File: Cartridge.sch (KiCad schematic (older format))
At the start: 1 part, among them J4 Expansion

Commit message: MMU, Joy, Cart and Video
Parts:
- added C18: 100nF, Atari:C_Axial_L5.1mm_D2.5mm_P12.50mm_Horizontal, symbol Device:C
- added J24: Cartridge, Atari:Cartridge_Slot, symbol Atari:Cartridge
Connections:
- net GND: now also C18.2, J24.B (GND)
- new net +5P: C18.1, J24.13 (VCC)
- new net A0: J24.5 (A0)
- new net A1: J24.4 (A1)
- new net A10: J24.P (A10)
- new net A11: J24.N (A11)
- new net A12: J24.K (A12)
- new net A2: J24.3 (A2)
- new net A3: J24.2 (A3)
- new net A4: J24.C (A4)
- new net A5: J24.D (A5)
- new net A6: J24.E (A6)
- new net A7: J24.F (A7)
- new net A8: J24.H (A8)
- new net A9: J24.J (A9)
- new net BO2: J24.S (O2)
- new net CCTL: J24.15 (~CCTL)
- new net D0: J24.10 (D0)
- new net D1: J24.9 (D1)
- new net D2: J24.8 (D2)
- new net D3: J24.L (D3)
- new net D4: J24.6 (D4)
- new net D5: J24.7 (D5)
- new net D6: J24.11 (D6)
- new net D7: J24.M (D7)
- new net RD4: J24.A (RD4)
- new net RD5: J24.14 (RDS)
- new net RW: J24.R (R/~W)
- new net S4: J24.1 (~S4)
- new net S5: J24.12 (~S5)
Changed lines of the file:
@@
 $Descr A4 11693 8268
 encoding utf-8
-Sheet 7 14
+Sheet 7 15
 Title ""
 Date ""
@@
 Wire Wire Line
 	3125 3950 3125 3750
+$Comp
+L Atari:Cartridge J24
+U 1 1 602F6C5A
+P 6700 3500
+F 0 "J24" H 6783 5215 50  0000 C CNN
+F 1 "Cartridge" H 6783 5124 50  0000 C CNN
+F 2 "Atari:Cartridge_Slot" H 7100 3450 50  0001 C CNN
+F 3 "" H 7100 3450 50  0001 C CNN
+	1    6700 3500
+	1    0    0    -1
+$EndComp
+Text GLabel 7000 2050 2    50   Input ~ 0
+A0
+Text GLabel 7000 2150 2    50   Input ~ 0
+A1
+Text GLabel 7000 2250 2    50   Input ~ 0
+A2
+Text GLabel 7000 2350 2    50   Input ~ 0
+A3
+Text GLabel 7000 2450 2    50   Input ~ 0
+A4
+Text GLabel 7000 2550 2    50   Input ~ 0
+A5
+Text GLabel 7000 2650 2    50   Input ~ 0
+A6
+Text GLabel 7000 2750 2    50   Input ~ 0
+A7
+Text GLabel 7000 2850 2    50   Input ~ 0
+A8
+Text GLabel 7000 2950 2    50   Input ~ 0
+A9
+Text GLabel 7000 3050 2    50   Input ~ 0
+A10
+Text GLabel 7000 3150 2    50   Input ~ 0
+A11
+Text GLabel 7000 3250 2    50   Input ~ 0
+A12
+Text GLabel 7000 3350 2    50   Input ~ 0
+D0
+Text GLabel 7000 3450 2    50   Input ~ 0
+D1
+Text GLabel 7000 3550 2    50   Input ~ 0
+D2
+Text GLabel 7000 3650 2    50   Input ~ 0
+D3
+Text GLabel 7000 3750 2    50   Input ~ 0
+D4
+Text GLabel 7000 3850 2    50   Input ~ 0
+D5
+Text GLabel 7000 3950 2    50   Input ~ 0
+D6
+Text GLabel 7000 4050 2    50   Input ~ 0
+D7
+Text GLabel 7000 4150 2    50   Input ~ 0
+S4
+Text GLabel 7000 4250 2    50   Input ~ 0
+S5
+Text GLabel 7000 4350 2    50   Input ~ 0
+RD5
+Text GLabel 7000 4450 2    50   Input ~ 0
+RD4
+Text GLabel 7000 4550 2    50   Input ~ 0
+CCTL
+Text GLabel 7000 4650 2    50   Input ~ 0
+RW
+Text GLabel 7000 4750 2    50   Input ~ 0
+BO2
+$Comp
+L power:+5P #PWR0197
+U 1 1 602F9620
+P 7475 4775
+F 0 "#PWR0197" H 7475 4625 50  0001 C CNN
+F 1 "+5P" H 7490 4948 50  0000 C CNN
+F 2 "" H 7475 4775 50  0001 C CNN
+F 3 "" H 7475 4775 50  0001 C CNN
+	1    7475 4775
+	1    0    0    -1
+$EndComp
+$Comp
+L Device:C C18
+U 1 1 602F9DE7
+P 7475 5000
+F 0 "C18" H 7590 5046 50  0000 L CNN
+F 1 "100nF" H 7590 4955 50  0000 L CNN
+F 2 "Atari:C_Axial_L5.1mm_D2.5mm_P12.50mm_Horizontal" H 7513 4850 50  0001 C CNN
+F 3 "~" H 7475 5000 50  0001 C CNN
+	1    7475 5000
+	1    0    0    -1
+$EndComp
+Wire Wire Line
+	7000 4850 7475 4850
+Wire Wire Line
+	7475 4775 7475 4850
+Connection ~ 7475 4850
+Wire Wire Line
+	7000 4950 7000 5150
+Wire Wire Line
+	7000 5150 7475 5150
+$Comp
+L power:GND #PWR0198
+U 1 1 602FAB68
+P 7475 5275
+F 0 "#PWR0198" H 7475 5025 50  0001 C CNN
+F 1 "GND" H 7480 5102 50  0000 C CNN
+F 2 "" H 7475 5275 50  0001 C CNN
+F 3 "" H 7475 5275 50  0001 C CNN
+	1    7475 5275
+	1    0    0    -1
+$EndComp
+Wire Wire Line
+	7475 5150 7475 5275
+Connection ~ 7475 5150
 $EndSCHEMATC

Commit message: Tracking
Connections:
- net +5P is gone; now on net +5VA: C18.1, J24.13 (VCC)
- net AUD renamed AUDIO
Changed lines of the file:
@@
 MPD
 Text GLabel 2650 3850 2    50   Input ~ 0
-AUD
+AUDIO
 $Comp
 L power:GND #PWR0143
@@
 BO2
 $Comp
-L power:+5P #PWR0197
-U 1 1 602F9620
-P 7475 4775
-F 0 "#PWR0197" H 7475 4625 50  0001 C CNN
-F 1 "+5P" H 7490 4948 50  0000 C CNN
-F 2 "" H 7475 4775 50  0001 C CNN
-F 3 "" H 7475 4775 50  0001 C CNN
-	1    7475 4775
-	1    0    0    -1
-$EndComp
-$Comp
 L Device:C C18
 U 1 1 602F9DE7
@@
 	7475 5150 7475 5275
 Connection ~ 7475 5150
+$Comp
+L power:+5VA #PWR0197
+U 1 1 602ED419
+P 7475 4775
+F 0 "#PWR0197" H 7475 4625 50  0001 C CNN
+F 1 "+5VA" H 7490 4948 50  0000 C CNN
+F 2 "" H 7475 4775 50  0001 C CNN
+F 3 "" H 7475 4775 50  0001 C CNN
+	1    7475 4775
+	1    0    0    -1
+$EndComp
 $EndSCHEMATC

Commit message: Tracking
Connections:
- net AUDIO renamed EXTAUDIO
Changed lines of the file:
@@
 MPD
 Text GLabel 2650 3850 2    50   Input ~ 0
-AUDIO
+EXTAUDIO
 $Comp
 L power:GND #PWR0143

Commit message: Diagnostic
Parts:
- added J212: Diag, Connector_PinHeader_2.54mm:PinHeader_2x05_P2.54mm_Vertical, symbol Connector_Generic:Conn_02x05_Odd_Even
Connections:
- net BO2: now also J212.1 (Pin_1)
- net CCTL: now also J212.3 (Pin_3)
- net D1XX: now also J212.4 (Pin_4)
- net GND: now also J212.10 (Pin_10)
- net RD4: now also J212.7 (Pin_7)
- net RD5: now also J212.2 (Pin_2)
- net RW: now also J212.8 (Pin_8)
- net S4: now also J212.5 (Pin_5)
- net S5: now also J212.9 (Pin_9)
- new net D6XX: J212.6 (Pin_6)
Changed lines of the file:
@@
+	1    0    0    -1
+$EndComp
+Text GLabel 5025 2900 2    50   Input ~ 0
+D1XX
+Text GLabel 4525 2800 0    50   Input ~ 0
+BO2
+Text GLabel 4525 2900 0    50   Input ~ 0
+CCTL
+Text GLabel 4525 3000 0    50   Input ~ 0
+S4
+Text GLabel 4525 3100 0    50   Input ~ 0
+RD4
+Text GLabel 4525 3200 0    50   Input ~ 0
+S5
+Text GLabel 5025 2800 2    50   Input ~ 0
+RD5
+Text GLabel 5025 3000 2    50   Input ~ 0
+D6XX
+Text GLabel 5025 3200 2    50   Input ~ 0
+GND
+Text GLabel 5025 3100 2    50   Input ~ 0
+RW
+$Comp
+L Connector_Generic:Conn_02x05_Odd_Even J212
+U 1 1 604245DE
+P 4725 3000
+F 0 "J212" H 4775 3417 50  0000 C CNN
+F 1 "Diag" H 4775 3326 50  0000 C CNN
+F 2 "Connector_PinHeader_2.54mm:PinHeader_2x05_P2.54mm_Vertical" H 4725 3000 50  0001 C CNN
+F 3 "~" H 4725 3000 50  0001 C CNN
+	1    4725 3000
 	1    0    0    -1
 $EndComp

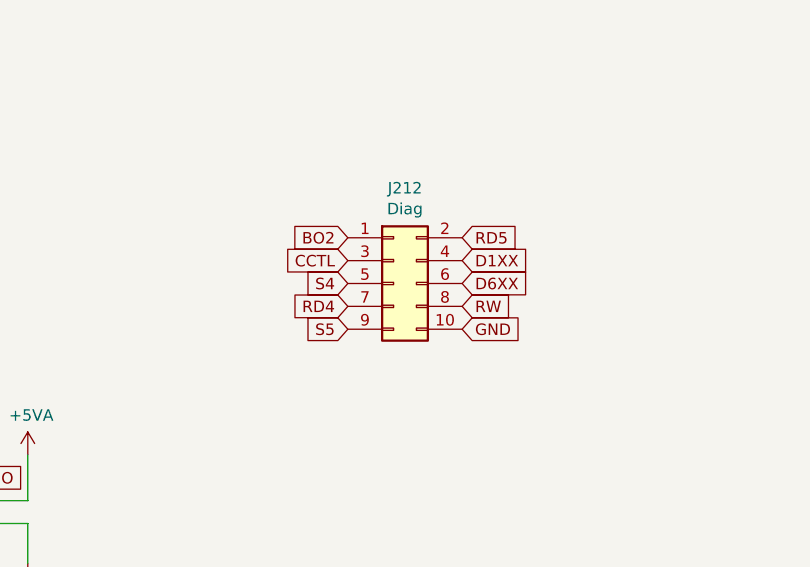
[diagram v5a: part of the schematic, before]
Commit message: Diagnostic pin
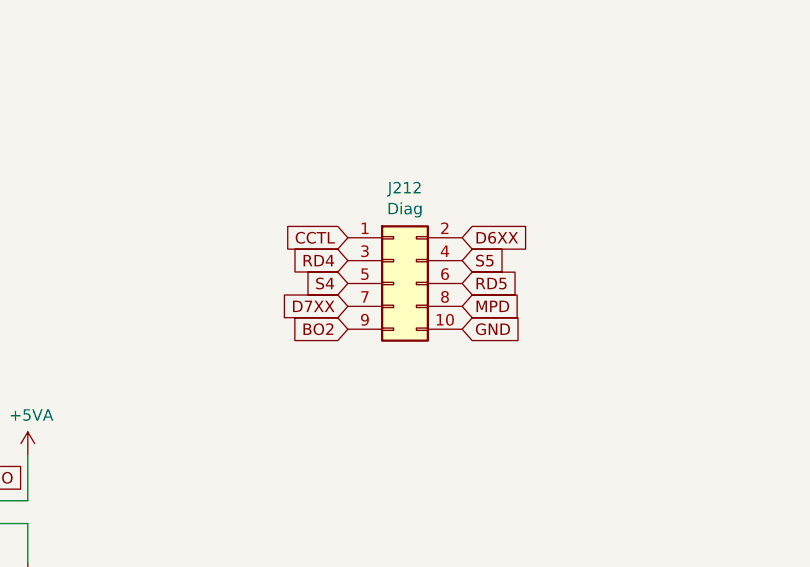
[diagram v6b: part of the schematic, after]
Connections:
- net BO2: now also J212.9 (Pin_9); no longer J212.1 (Pin_1)
- net CCTL: now also J212.1 (Pin_1); no longer J212.3 (Pin_3)
- net D1XX: no longer J212.4 (Pin_4)
- net D6XX: now also J212.2 (Pin_2); no longer J212.6 (Pin_6)
- net MPD: now also J212.8 (Pin_8)
- net RD4: now also J212.3 (Pin_3); no longer J212.7 (Pin_7)
- net RD5: now also J212.6 (Pin_6); no longer J212.2 (Pin_2)
- net RW: no longer J212.8 (Pin_8)
- net S5: now also J212.4 (Pin_4); no longer J212.9 (Pin_9)
- new net D7XX: J212.7 (Pin_7)
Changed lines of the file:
@@
 	1    0    0    -1
 $EndComp
-Text GLabel 5025 2900 2    50   Input ~ 0
-D1XX
+Text GLabel 4525 3100 0    50   Input ~ 0
+D7XX
+Text GLabel 4525 3200 0    50   Input ~ 0
+BO2
 Text GLabel 4525 2800 0    50   Input ~ 0
-BO2
-Text GLabel 4525 2900 0    50   Input ~ 0
 CCTL
 Text GLabel 4525 3000 0    50   Input ~ 0
 S4
-Text GLabel 4525 3100 0    50   Input ~ 0
+Text GLabel 4525 2900 0    50   Input ~ 0
 RD4
-Text GLabel 4525 3200 0    50   Input ~ 0
+Text GLabel 5025 2900 2    50   Input ~ 0
 S5
+Text GLabel 5025 3000 2    50   Input ~ 0
+RD5
 Text GLabel 5025 2800 2    50   Input ~ 0
-RD5
-Text GLabel 5025 3000 2    50   Input ~ 0
 D6XX
 Text GLabel 5025 3200 2    50   Input ~ 0
 GND
 Text GLabel 5025 3100 2    50   Input ~ 0
-RW
+MPD
 $Comp
 L Connector_Generic:Conn_02x05_Odd_Even J212

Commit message: Tracking
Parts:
- removed J212: Diag, Connector_PinHeader_2.54mm:PinHeader_2x05_P2.54mm_Vertical, symbol Connector_Generic:Conn_02x05_Odd_Even
- added J212: Diag, Connector_PinHeader_2.54mm:PinHeader_2x06_P2.54mm_Vertical, symbol Connector_Generic:Conn_02x06_Odd_Even
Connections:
- net BO2: now also J212.12 (Pin_12)
- net CCTL: now also J212.1 (Pin_1)
- net D6XX: now also J212.2 (Pin_2)
- net D7XX: now also J212.7 (Pin_7)
- net GND: now also J212.11 (Pin_11), J212.9 (Pin_9)
- net MPD: now also J212.8 (Pin_8)
- net RD4: now also J212.3 (Pin_3)
- net RD5: now also J212.6 (Pin_6)
- net RST: now also J212.10 (Pin_10)
- net S4: now also J212.5 (Pin_5)
- net S5: now also J212.4 (Pin_4)
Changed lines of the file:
@@
 Text GLabel 4525 3100 0    50   Input ~ 0
 D7XX
-Text GLabel 4525 3200 0    50   Input ~ 0
+Text GLabel 5025 3300 2    50   Input ~ 0
 BO2
 Text GLabel 4525 2800 0    50   Input ~ 0
@@
 D6XX
 Text GLabel 5025 3200 2    50   Input ~ 0
-GND
+RST
 Text GLabel 5025 3100 2    50   Input ~ 0
 MPD
 $Comp
-L Connector_Generic:Conn_02x05_Odd_Even J212
-U 1 1 604245DE
+L Connector_Generic:Conn_02x06_Odd_Even J212
+U 1 1 604B3554
 P 4725 3000
 F 0 "J212" H 4775 3417 50  0000 C CNN
 F 1 "Diag" H 4775 3326 50  0000 C CNN
-F 2 "Connector_PinHeader_2.54mm:PinHeader_2x05_P2.54mm_Vertical" H 4725 3000 50  0001 C CNN
+F 2 "Connector_PinHeader_2.54mm:PinHeader_2x06_P2.54mm_Vertical" H 4725 3000 50  0001 C CNN
 F 3 "~" H 4725 3000 50  0001 C CNN
 	1    4725 3000
 	1    0    0    -1
 $EndComp
+$Comp
+L power:GND #PWR?
+U 1 1 604B4D92
+P 4525 3425
+F 0 "#PWR?" H 4525 3175 50  0001 C CNN
+F 1 "GND" H 4530 3252 50  0000 C CNN
+F 2 "" H 4525 3425 50  0001 C CNN
+F 3 "" H 4525 3425 50  0001 C CNN
+	1    4525 3425
+	1    0    0    -1
+$EndComp
+Wire Wire Line
+	4525 3200 4525 3300
+Wire Wire Line
+	4525 3300 4525 3425
+Connection ~ 4525 3300
 $EndSCHEMATC
